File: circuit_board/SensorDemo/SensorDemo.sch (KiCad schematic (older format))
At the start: 61 parts, among them U1 TLV1117-33CDCYR, U2 dsPIC33EP32GP502, U4 INA126

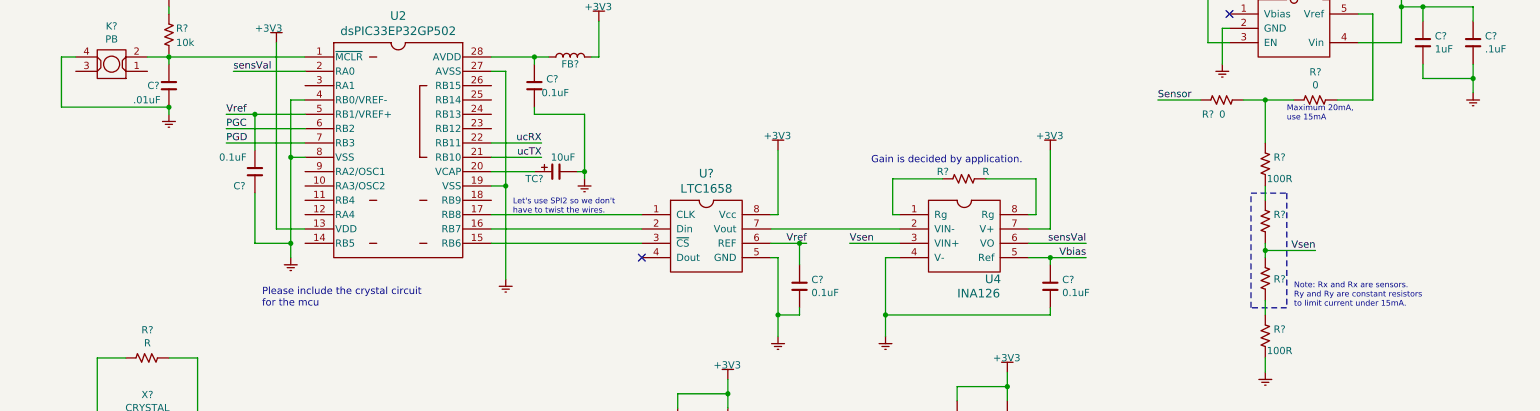
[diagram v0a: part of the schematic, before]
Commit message: minor update
ft231 breakout board added under reference folder.
minor update on schematic.
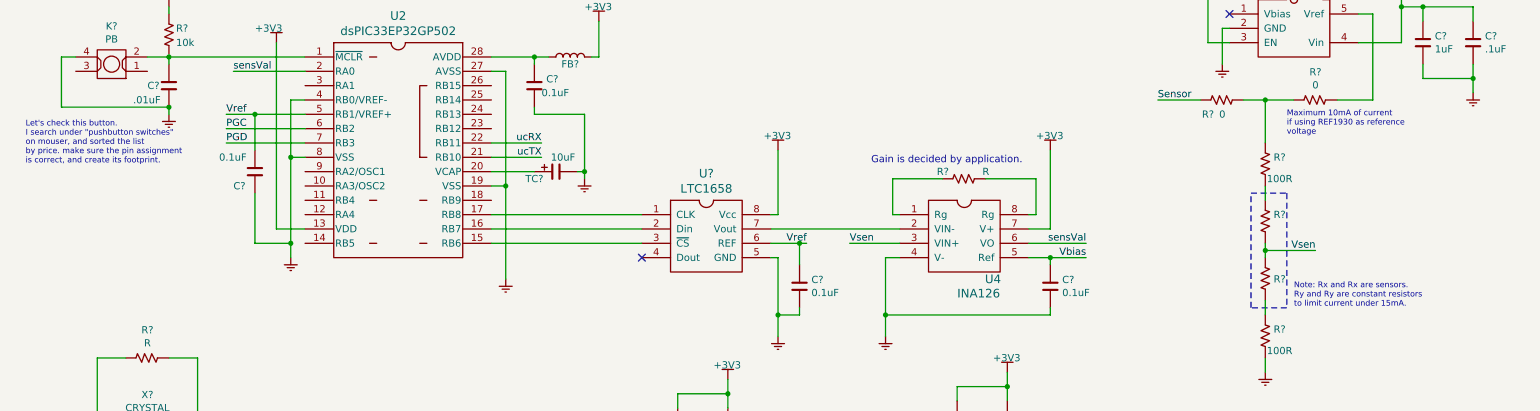
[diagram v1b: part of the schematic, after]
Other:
- note added: "Let's check this button. \nI search under "pushbutton switches"\non mouser, and sorted the list\nby price. make sure the pin assignment\nis correct, and create its footprint."
- note added: "Maximum 10mA of current\nif using REF1930 as reference\nvoltage"
- note removed: "Let's use SPI2 so we don't\nhave to twist the wires."
- note removed: "Maximum 20mA,\nuse 15mA"
- note removed: "Please include the crystal circuit\nfor the mcu"
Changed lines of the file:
@@
 F 1 "PB" H 1250 2276 50  0000 C CNN
 F 2 "" H 1250 2300 60  0001 C CNN
-F 3 "https://www.mouser.com/ProductDetail/Schurter/1241161211?qs=JHn%2F0Af%2Fl5HGUVmYq1Th2w%3D%3D" H 1250 2300 60  0001 C CNN
+F 3 "https://www.mouser.com/ProductDetail/E-Switch/LL3301NF065QG/?qs=QtyuwXswaQiWhwgY68YTTw%3D%3D" H 1250 2300 60  0001 C CNN
 	1    1250 2450
 	-1   0    0    1
@@
 Wire Wire Line
 	4950 3500 3900 3500
-Text Notes 4050 3500 0    40   ~ 0
-Let's use SPI2 so we don't\nhave to twist the wires.
 Text Notes 10650 850  0    40   ~ 0
 Note:\nVref = 3V\nVbias = 1.5V
@@
 Wire Wire Line
 	10050 2100 10050 2700
-Text Notes 9450 2850 0    40   ~ 0
-Maximum 20mA,\nuse 15mA
+Text Notes 9450 2950 0    40   ~ 0
+Maximum 10mA of current\nif using REF1930 as reference\nvoltage
 $Comp
 L SensorDemo_passive:FB FB?
@@
 Wire Wire Line
 	5900 4200 5900 3800
-Text Notes 2300 4150 0    50   ~ 0
-Please include the crystal circuit\nfor the mcu
 Text Notes 6550 3150 0    50   ~ 0
 Gain is decided by application.
@@
 	9500 2700 9300 2700
 Connection ~ 9300 2700
+Text Notes 650  3150 0    40   ~ 0
+Let's check this button. \nI search under "pushbutton switches"\non mouser, and sorted the list\nby price. make sure the pin assignment\nis correct, and create its footprint.
 $EndSCHEMATC

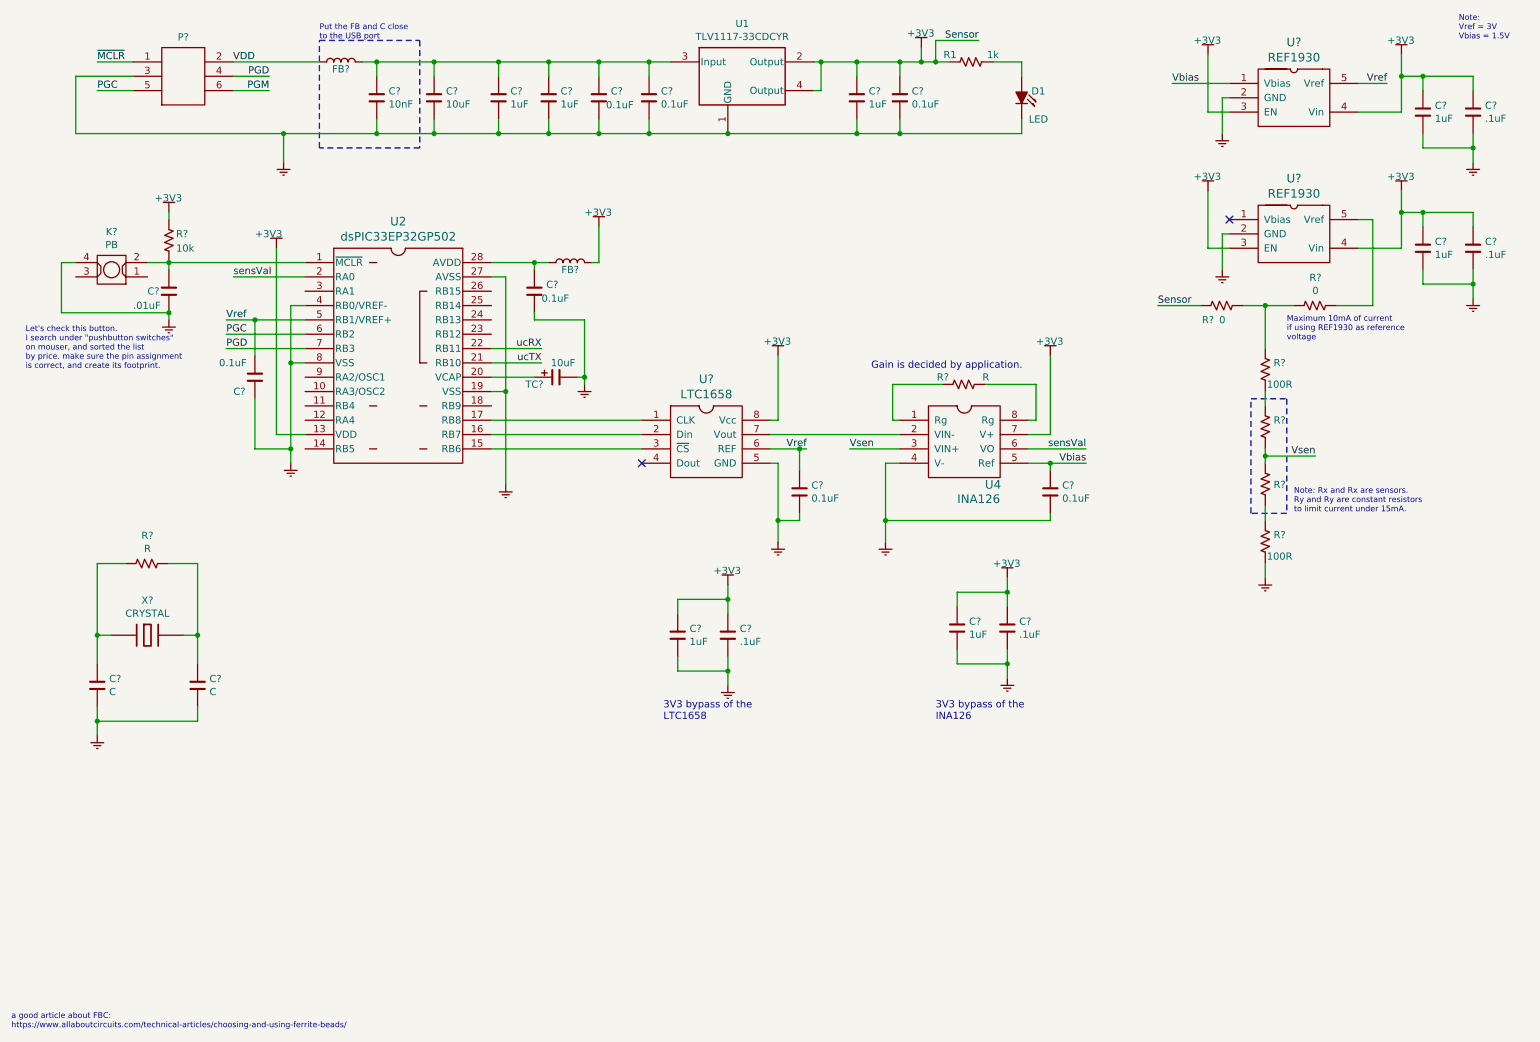
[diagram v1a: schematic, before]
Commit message: updated schematic
added footprints to everything and minor changes to 6pin
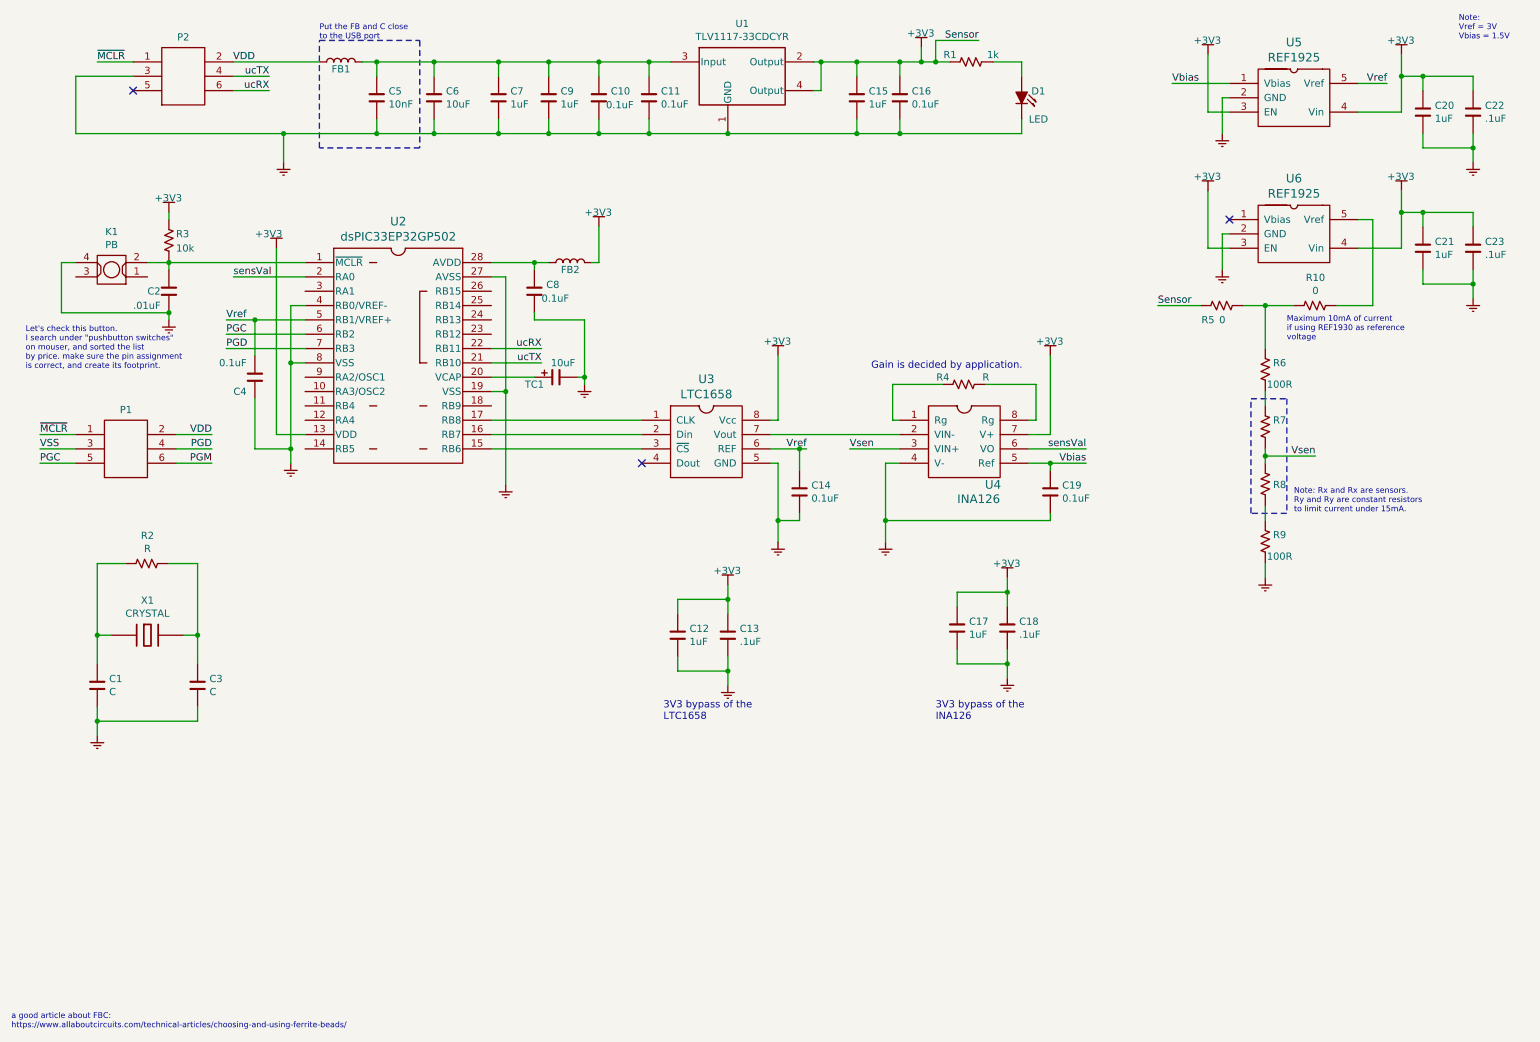
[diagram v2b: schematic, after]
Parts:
- removed PS? (x9): GND, symbol SensorDemo_power_supply:GND
- removed PS? (x6): +3V3, symbol SensorDemo_power_supply:+3V3
- added P1: CONN3X2, symbol SensorDemo_connector:CONN3X2
- C1, C10, C11, C12, C13, C14, C15, C16, C17, C18, C19, C2, C20, C21, C22, C23, C3, C4, C5, C6, C7, C8, C9: renamed from C?; footprint (none) -> SensorDemo_pcb:C0805
- K1: renamed from K?; footprint (none) -> SensorDemo_pcb:SOT-23-4
- R10, R2, R3, R4, R5, R6, R9: renamed from R?; footprint (none) -> SensorDemo_pcb:R0805
- U3: renamed from U?; footprint (none) -> SensorDemo_pcb:SOIC-8
- U4: footprint SensorDemo_pcb:DIP_8_300 -> SensorDemo_pcb:SOIC-8
- U5, U6: renamed from U?; value REF1930 -> REF1925; footprint (none) -> SensorDemo_pcb:SOT-23-5
- X1: renamed from X?; footprint (none) -> SensorDemo_pcb:CRYSTAL_ABM3-8.000MHz-D2Y-T
- gave numbers to parts that had none: 6
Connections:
- net PGC: now also P1.5; no longer P2.5
- net PGD: now also P1.4; no longer P2.4
- net PGM: now also P1.6; no longer P2.6
- net VDD: now also P1.2
- net ucRX: now also P2.6
- net ucTX: now also P2.4
- net ~MCLR: now also P1.1
- new net VSS: P1.3
- no-connect marks 2 -> 3

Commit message: updated schematic
added footprints & created footprint for connector
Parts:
- P1, P2: footprint (none) -> SensorDemo_pcb:TC2030
- TC1: footprint (none) -> SensorDemo_pcb:C1210; link https://www.mouser.com/ProductDetail/AVX/TAJB106K020SNJ/?qs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 -> (none)
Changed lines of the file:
@@
 F 0 "TC1" H 4200 3150 50  0000 C CNN
 F 1 "10uF" H 4400 3300 50  0000 C CNN
-F 2 "" H 4388 3050 30  0001 C CNN
-F 3 "" H 4350 3200 60  0000 C CNN
-F 4 "https://www.mouser.com/ProductDetail/AVX/TAJB106K020SNJ/?qs=sGAEpiMZZMtZ1n0r9vR22dqqeipQnnsBpy1lZYztj8Q%3D" H 4350 3200 50  0001 C CNN "link"
+F 2 "SensorDemo_pcb:C1210" H 4388 3050 30  0001 C CNN
+F 3 "https://www.mouser.com/ProductDetail/AVX/TAJB106K020SNJ/?qs=sGAEpiMZZMtZ1n0r9vR22dqqeipQnnsBpy1lZYztj8Q%3D" H 4350 3200 60  0001 C CNN
 	1    4350 3200
 	1    0    0    -1
@@
 F 0 "P2" H 1750 1373 50  0000 C CNN
 F 1 "CONN3X2" H 1750 650 50  0001 C CNN
-F 2 "" H 5050 -1050 60  0001 C CNN
+F 2 "SensorDemo_pcb:TC2030" H 5050 -1050 60  0001 C CNN
 F 3 "" H 5050 -1050 60  0000 C CNN
 	1    1750 1100
@@
 F 0 "P1" H 1350 3973 50  0000 C CNN
 F 1 "CONN3X2" H 1350 3250 50  0001 C CNN
-F 2 "" H 4650 1550 60  0001 C CNN
-F 3 "" H 4650 1550 60  0000 C CNN
+F 2 "SensorDemo_pcb:TC2030" H 4650 1550 60  0001 C CNN
+F 3 "" H 4650 1550 60  0001 C CNN
 	1    1350 3700
 	1    0    0    -1

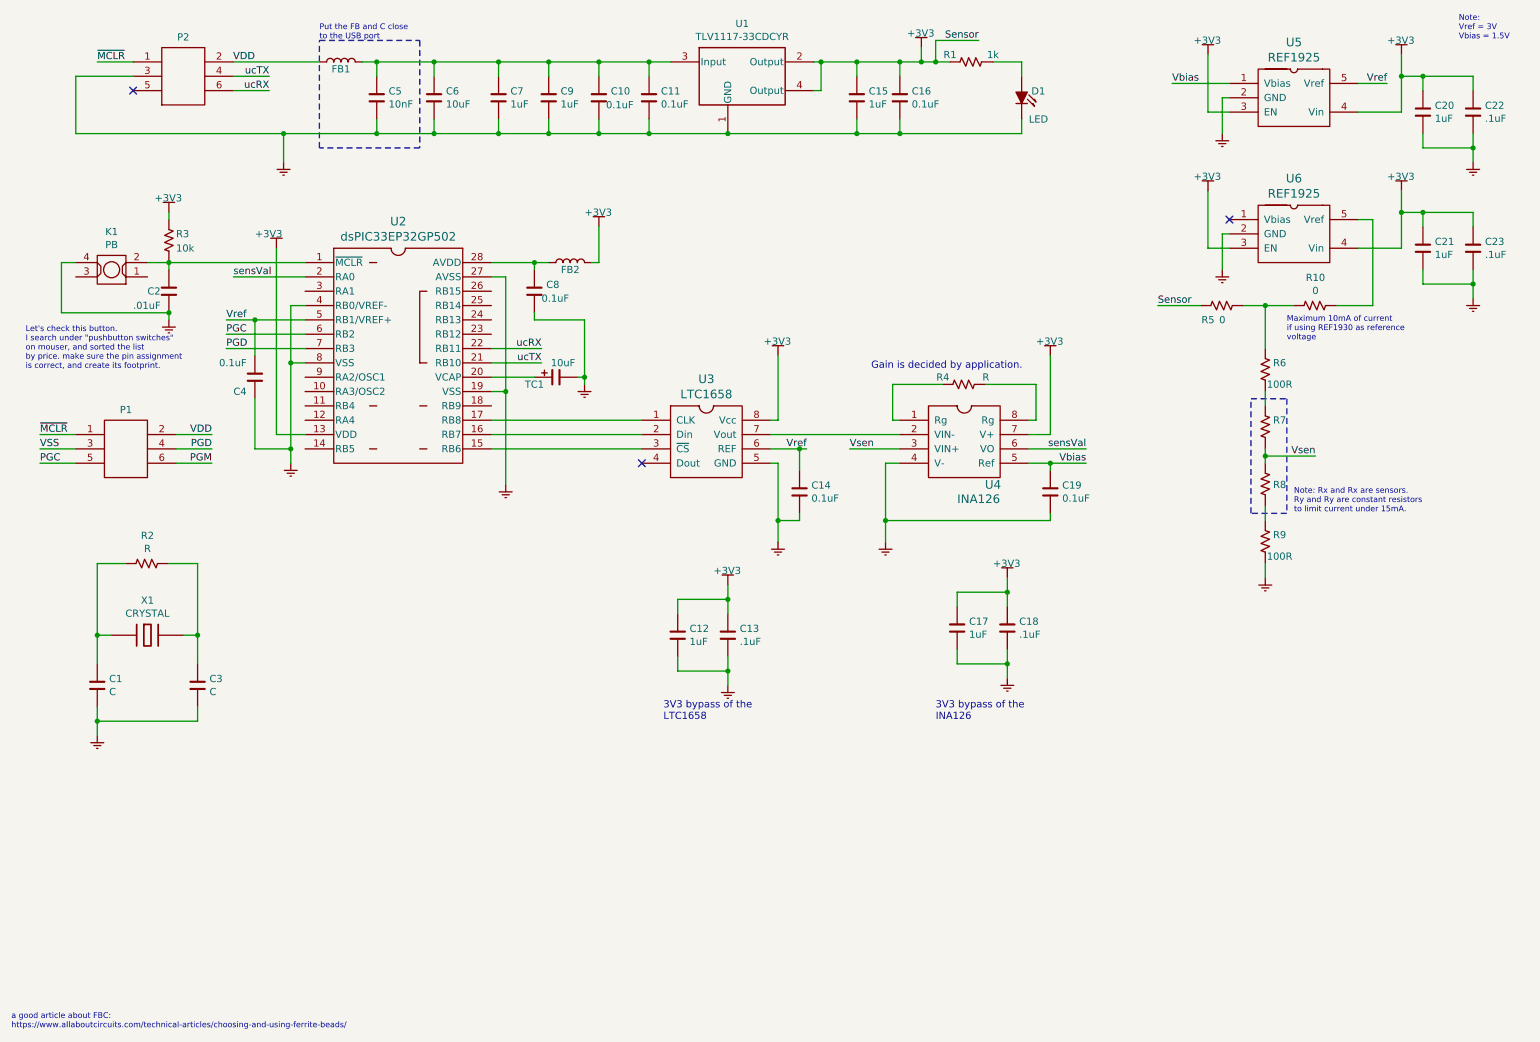
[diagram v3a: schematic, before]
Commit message: minor change on schematic
please add pads to the 6 pin connector.
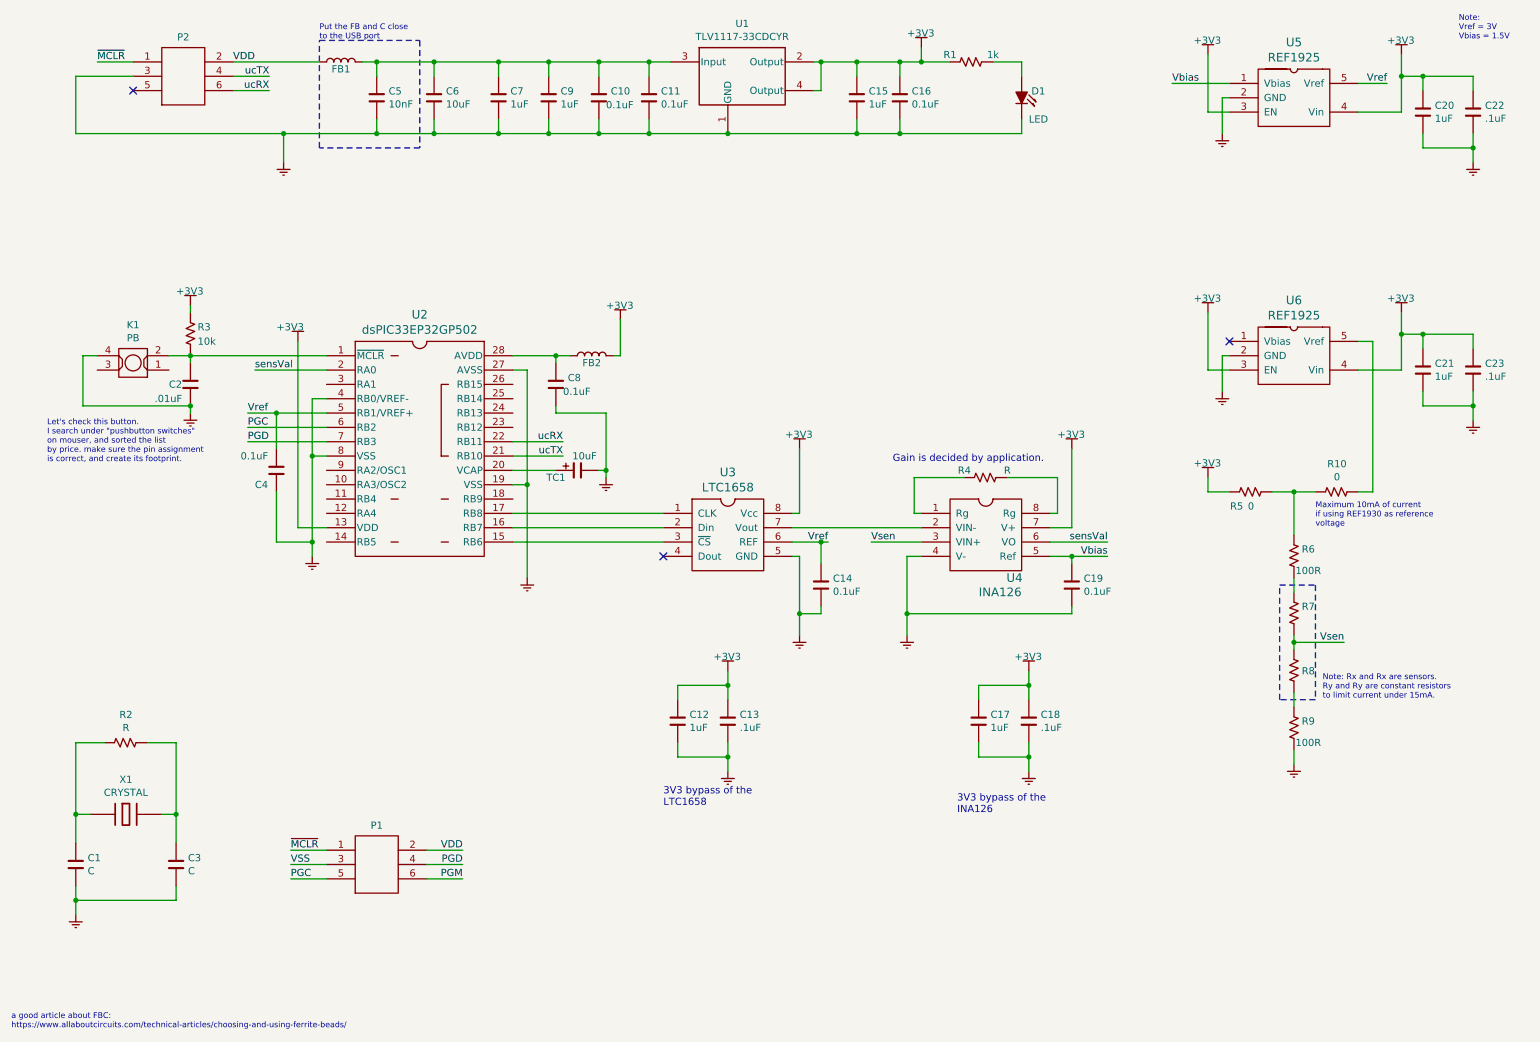
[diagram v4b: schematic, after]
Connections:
- net Sensor: no longer names the net of C15.1, C16.1, R1.1, U1.2 (Output), U1.4 (Output)
- net Sensor: no longer R5.1
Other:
- moved on the sheet: C1, C12, C13, C14, C17, C18, C19, C2, C21, C23, C3, C4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
